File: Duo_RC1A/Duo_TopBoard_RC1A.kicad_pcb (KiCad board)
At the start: 2 copper layers, 169.2 x 131.9 mm, 110 parts, among them CN1 CONN_PANNEL_2X2, CN2 CONN_PANNEL_2X2, P1 HEADER_180_2.54_10X2, P2 KK3.96_2, P3 HEADER_180_2.54_4X1, P4 HEADER_180_2.54_5X2, Q1 MMBT3904, Q2 MMBT3904, SW1 SW_PUSH, U1 LPC1754FBD80, U2 TLV803, U3 74LVC1G125, U4 NCP1117DT33G, X1 10MHz

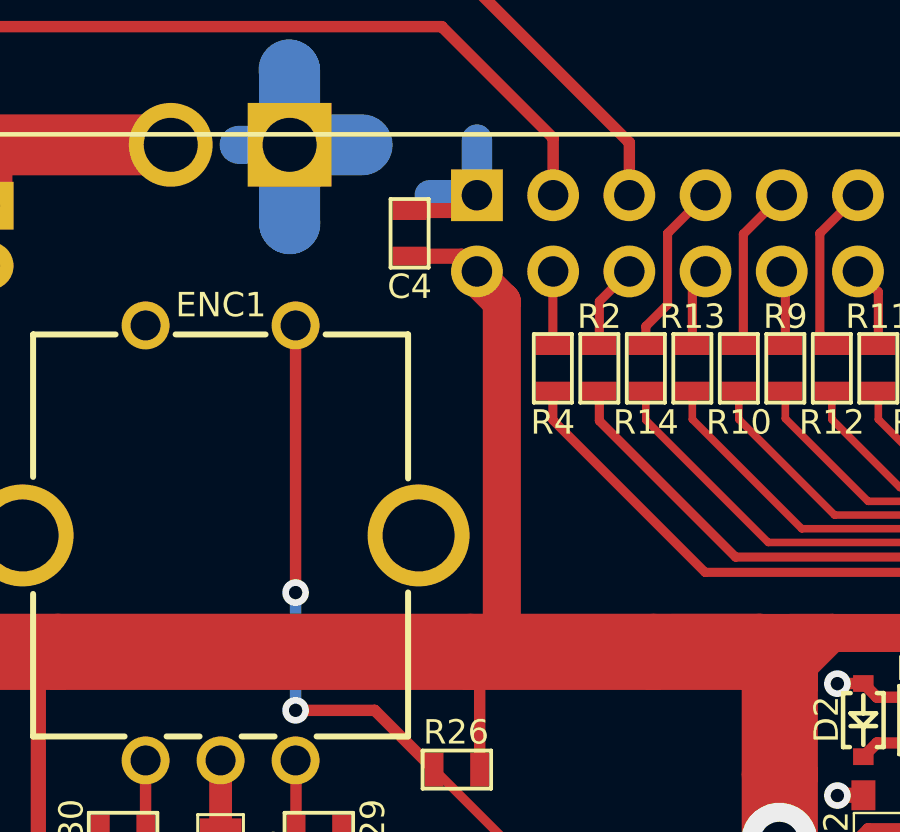
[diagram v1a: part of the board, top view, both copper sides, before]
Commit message: USB OTG and HOST traks done.
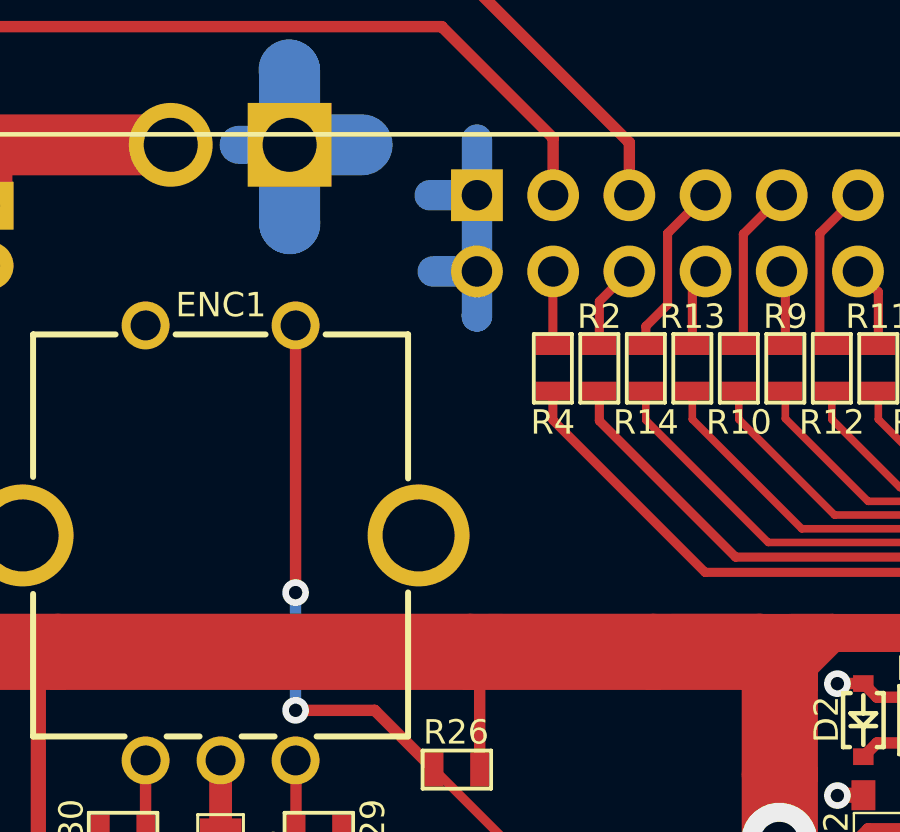
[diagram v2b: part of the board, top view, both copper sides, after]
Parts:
- removed C4: 100nF_X7R, Duo_Audio_HMI_RC1A:SM0603
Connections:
- P1 pad 2: +3.3V -> DGND
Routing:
- net +3.3V: track 797.2 -> 782.3 mm
- net DGND: track 99.6 -> 102.7 mm

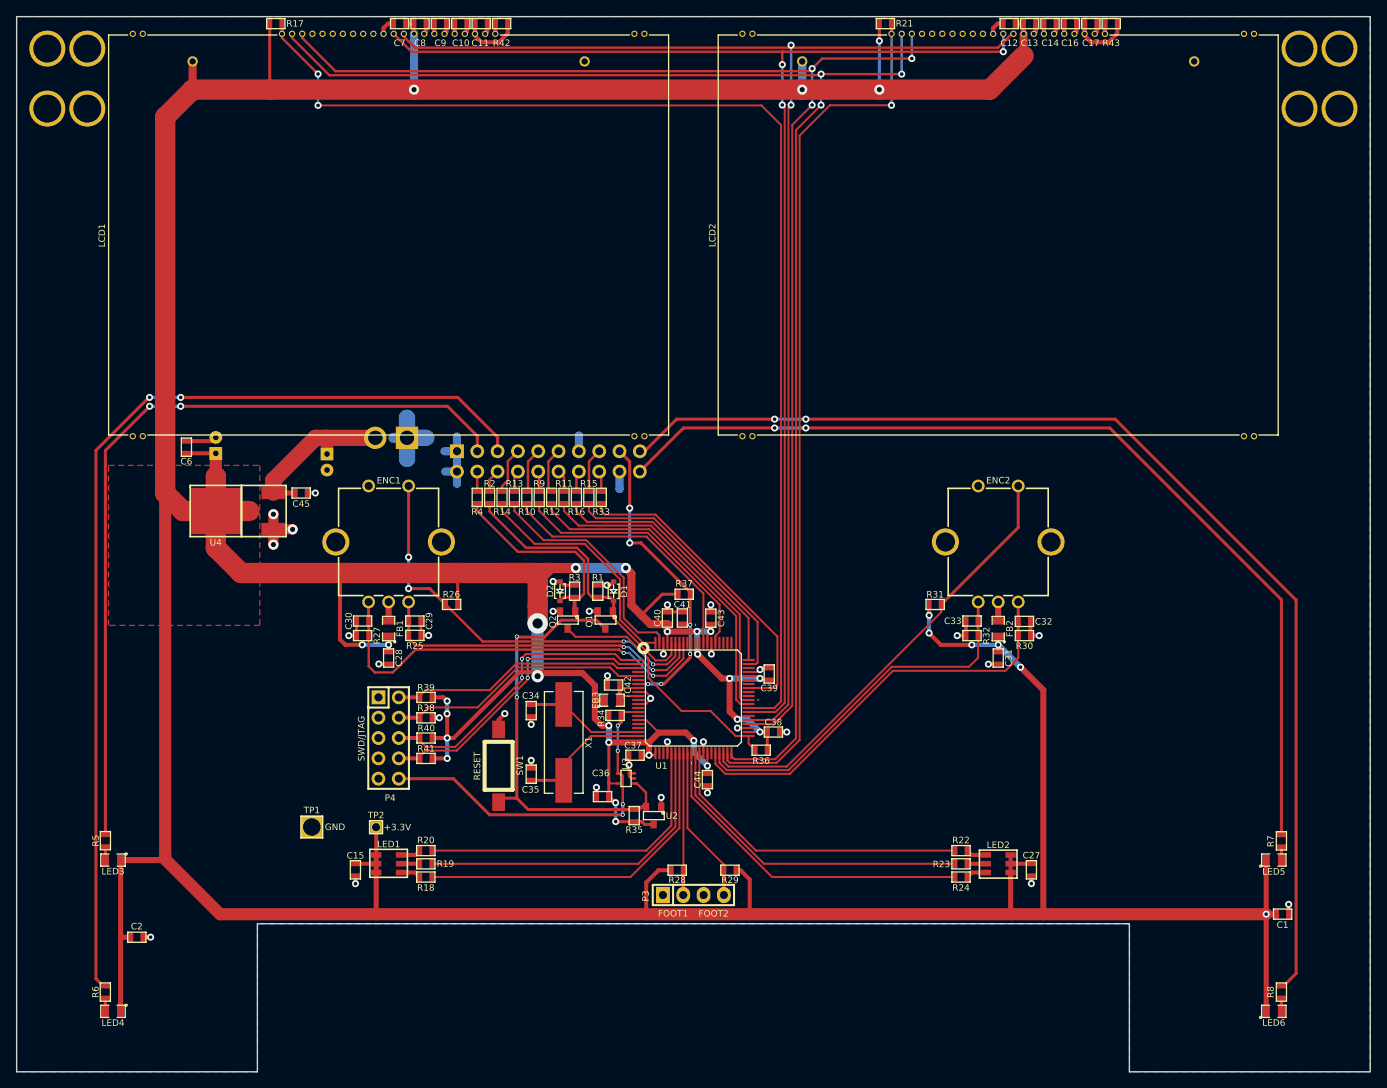
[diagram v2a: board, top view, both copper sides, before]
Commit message: Included the *.fex file for ITEAD A20. Included the BOM of the two boards togheter. Completed the BOM of both boards.
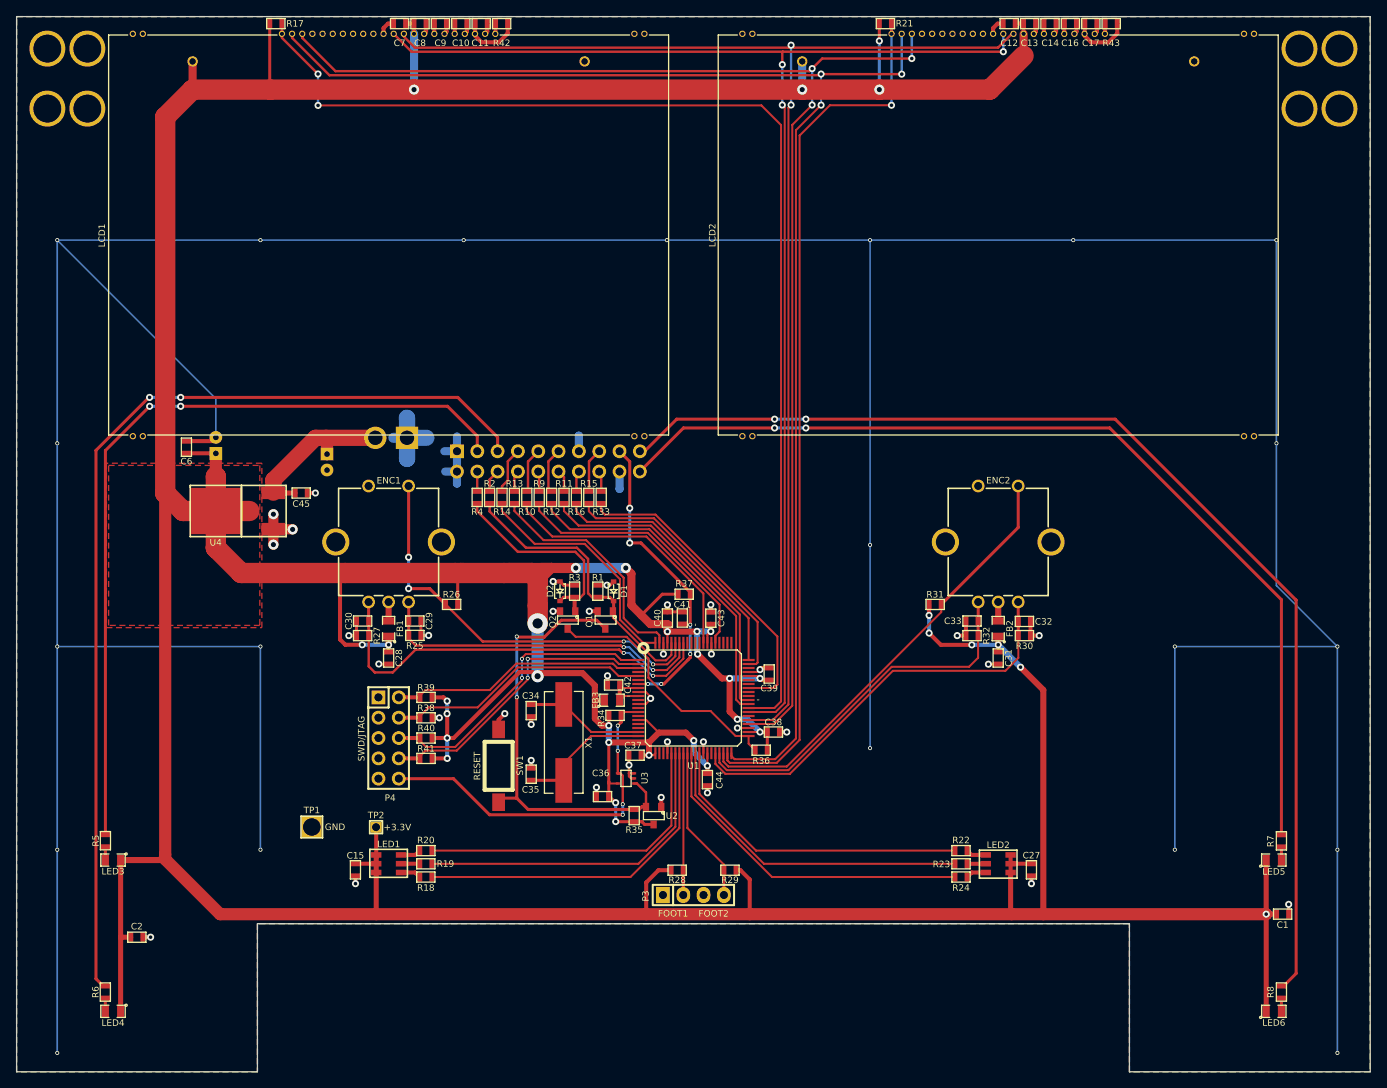
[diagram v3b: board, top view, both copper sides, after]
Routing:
- net DGND: track 102.7 -> 654.3 mm, vias 37 -> 58
- added copper zone on F.Cu, net DGND

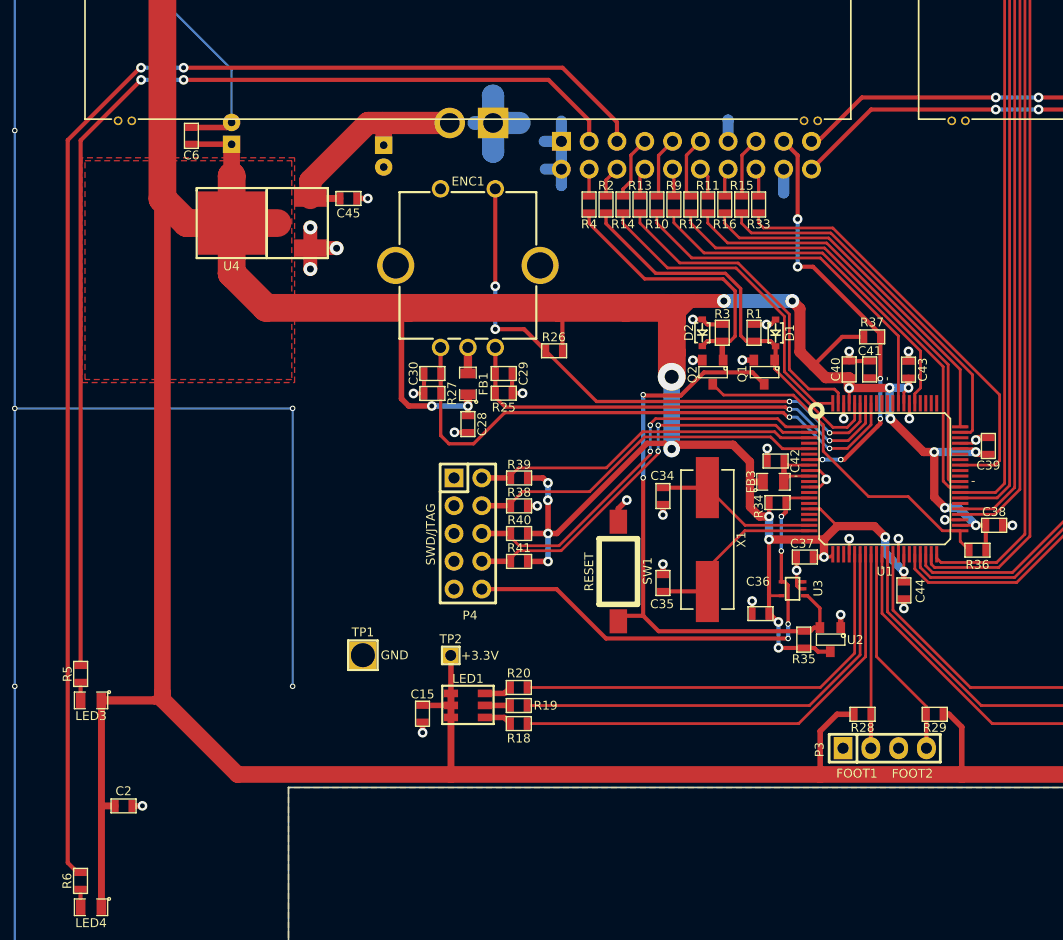
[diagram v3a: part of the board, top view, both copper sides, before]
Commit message: Fixed issue #3: re-traced the signals on the TopBoard for the flipped HMI flat cable connector.
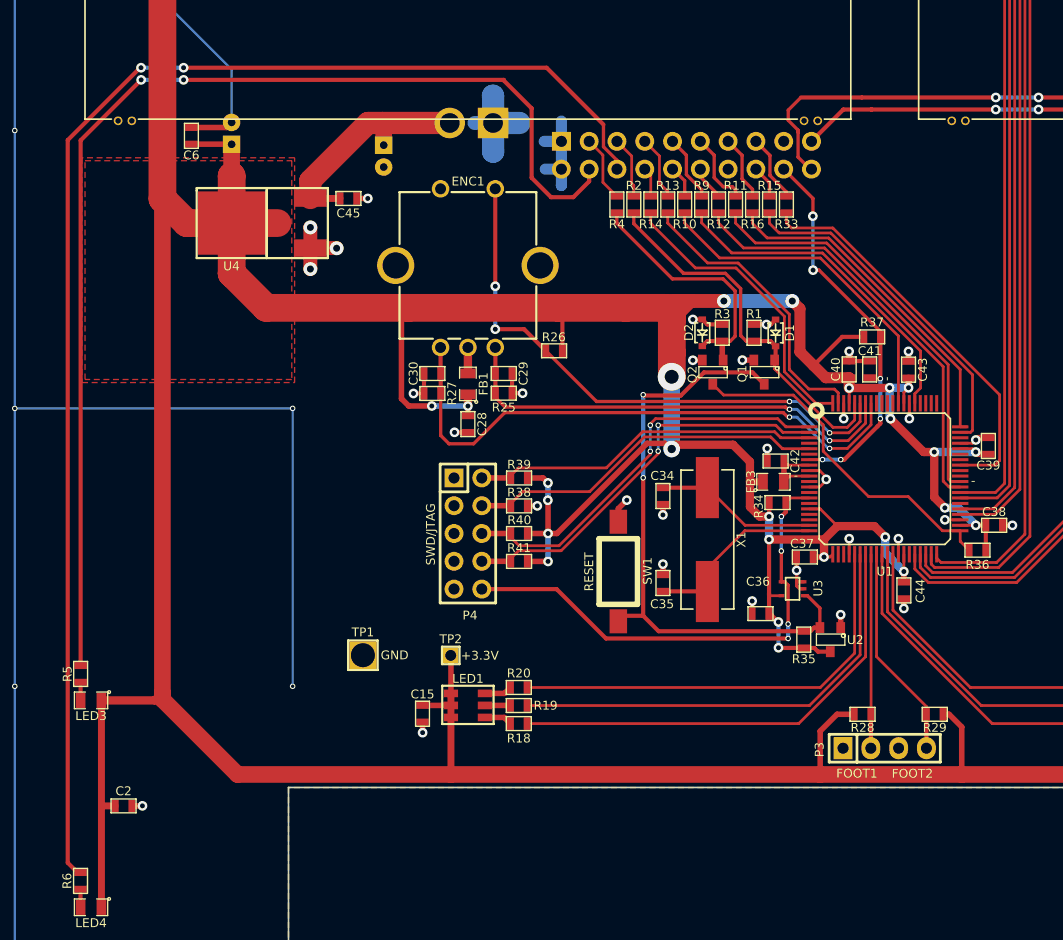
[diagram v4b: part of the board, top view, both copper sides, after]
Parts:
- moved R10 2.54 mm to (88.7, 85.5)
- moved R12 2.54 mm to (91.8, 85.5)
- moved R15 2.54 mm to (96.4, 85.5)
- moved R2 2.54 mm to (84.0, 85.5)
- moved R33 2.54 mm to (98.0, 85.5)
- moved R4 2.54 mm to (82.5, 85.5)
- moved R9 2.54 mm to (90.2, 85.5)
- moved R11 2.54 mm to (93.3, 85.5)
- moved R13 2.54 mm to (87.1, 85.5)
- moved R14 2.54 mm to (85.6, 85.5)
- moved R16 2.54 mm to (94.9, 85.5)
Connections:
- P1 pad 13: DGND -> Net-(P1-Pad13)
- P1 pad 14: Net-(P1-Pad14) -> DGND
- P1 pad 17: NTC_TEMP -> DGND
- P1 pad 18: DGND -> NTC_TEMP
- P1 pad 19: LED_OVFL4 -> LED_OVFL3
- P1 pad 20: LED_OVFL3 -> LED_OVFL4
- P1 pad 3: LED_OVFL1 -> RTS_HOST_FIRMWARE
- P1 pad 4: RTS_HOST_FIRMWARE -> LED_OVFL1
- P1 pad 5: LED_OVFL2 -> DTR_HOST_FIRMWARE
- P1 pad 6: DTR_HOST_FIRMWARE -> LED_OVFL2
- R10 pad 2: Net-(P1-Pad9) -> Net-(P1-Pad10)
- R11 pad 2: Net-(P1-Pad12) -> Net-(P1-Pad11)
- R12 pad 2: Net-(P1-Pad11) -> Net-(P1-Pad12)
- R13 pad 2: Net-(P1-Pad8) -> Net-(P1-Pad7)
- R14 pad 2: Net-(P1-Pad7) -> Net-(P1-Pad8)
- R15 pad 2: Net-(P1-Pad15) -> Net-(P1-Pad16)
- R16 pad 2: Net-(P1-Pad14) -> Net-(P1-Pad13)
- R33 pad 2: Net-(P1-Pad16) -> Net-(P1-Pad15)
- R9 pad 2: Net-(P1-Pad10) -> Net-(P1-Pad9)
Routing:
- net LED_OVFL4: track 142.2 -> 149.5 mm
- net LED_OVFL1: track 100.2 -> 106.7 mm
- net Net-(P1-Pad13): track 0.00 -> 5.93 mm
- net DGND: track 654.3 -> 650.6 mm
- net RTS_HOST_FIRMWARE: track 2.47 -> 6.06 mm
- net NTC_TEMP: track 39.3 -> 36.5 mm
- net DTR_HOST_FIRMWARE: track 2.88 -> 5.65 mm
- net Net-(P1-Pad14): track 2.60 -> 0.00 mm
- net RXD3_UC_CONSOLE: track 33.4 -> 30.9 mm
- net RXD2_UC_UI: track 41.7 -> 39.1 mm
- net RX1_UC_CHAIN: track 34.1 -> 31.5 mm
- net RTS1_UC_CHAIN: track 39.2 -> 36.7 mm
- net RESET_UC_EN: track 37.3 -> 34.8 mm
- net Net-(D2-Pad2): track 26.2 -> 23.6 mm
- net TXD3_UC_CONSOLE: track 33.3 -> 30.8 mm
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
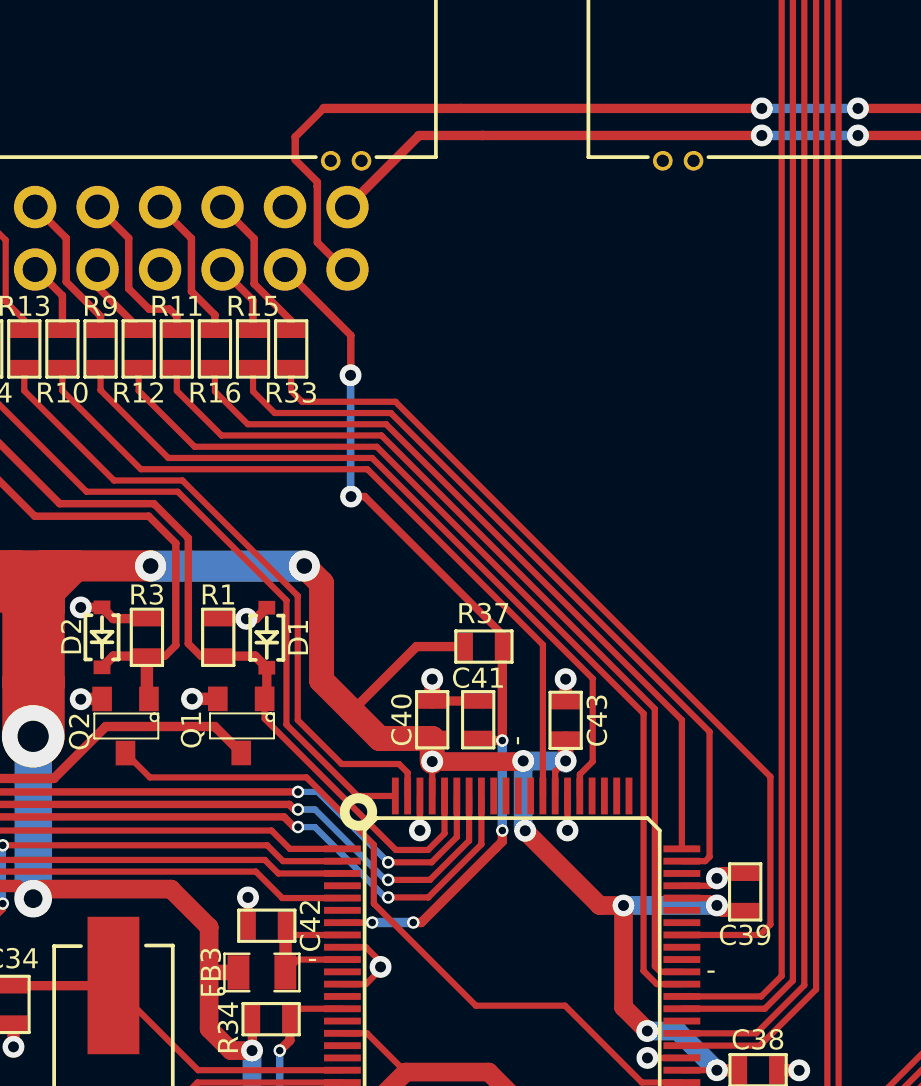
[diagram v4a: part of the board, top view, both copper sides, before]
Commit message: wip issue #14: updated traces on TopBoard. Still pending: same for BottomBoard.
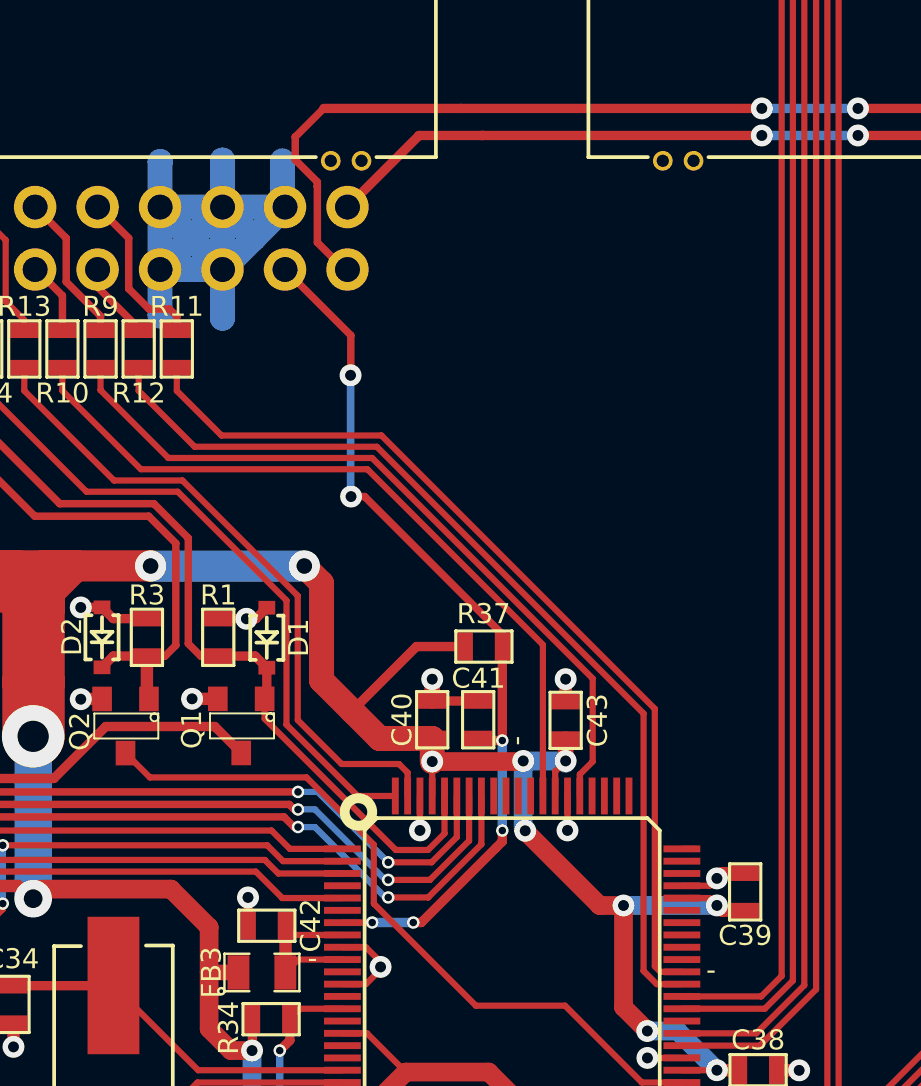
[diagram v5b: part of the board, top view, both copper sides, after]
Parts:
- removed R15, R16, R33: 100R, Duo_Audio_HMI_RC1A:SM0603
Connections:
- P1 pad 13: Net-(P1-Pad13) -> DGND
- P1 pad 15: Net-(P1-Pad15) -> DGND
- P1 pad 16: Net-(P1-Pad16) -> DGND
- U1 pad 53: RTS1_UC_CHAIN -> Net-(U1-Pad53)
- U1 pad 59: RX1_UC_CHAIN -> Net-(U1-Pad59)
- U1 pad 60: TX1_UC_CHAIN -> Net-(U1-Pad60)
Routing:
- net RTS1_UC_CHAIN: track 36.7 -> 0.00 mm
- net DGND: track 650.6 -> 685.9 mm
- net RX1_UC_CHAIN: track 31.5 -> 0.00 mm
- net TX1_UC_CHAIN: track 31.3 -> 0.00 mm
- net Net-(P1-Pad15): track 6.17 -> 0.00 mm
- net Net-(P1-Pad13): track 5.93 -> 0.00 mm
- net Net-(P1-Pad16): track 3.37 -> 0.00 mm
- net Net-(U1-Pad60): track 0.00 -> 0.60 mm
